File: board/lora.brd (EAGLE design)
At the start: 20.2 x 72.9 mm, 29 parts, among them J1 SWD_PTH_SHROUD, X1 SMA-142-0701-801/806

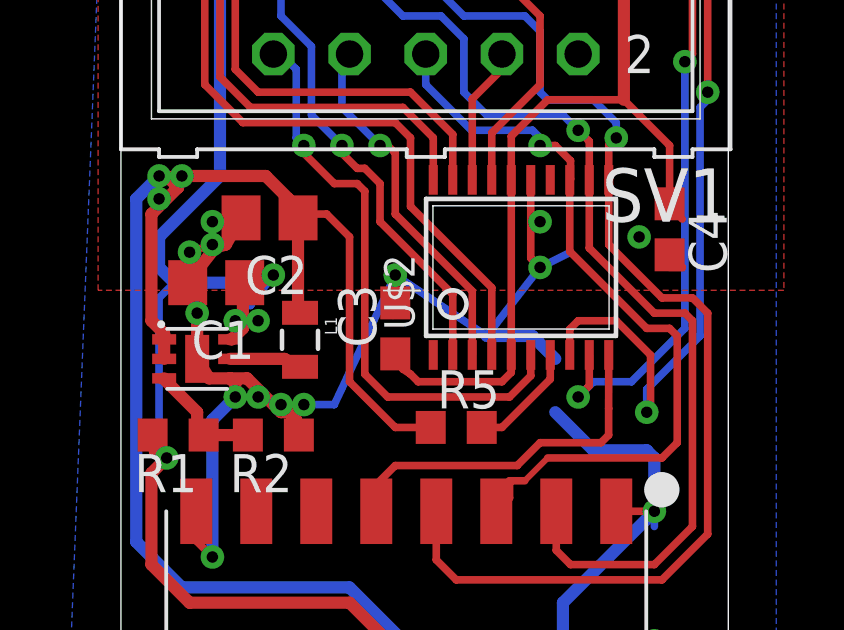
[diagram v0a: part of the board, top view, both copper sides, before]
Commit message: added boot0 to tracker, some wiring on basestation
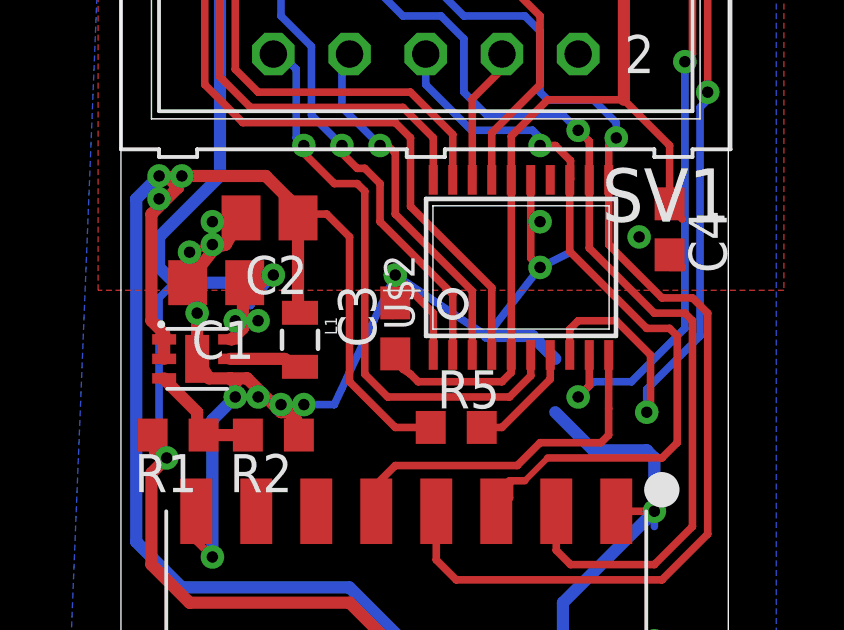
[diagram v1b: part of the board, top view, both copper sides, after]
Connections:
- net GND: now also U$2.1
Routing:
- net GND: track 95.3 -> 98.5 mm
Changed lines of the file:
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@@
 <via x="15.875" y="48.387" extent="1-16" drill="0.381" shape="octagon"/>
 <contactref element="TP2" pad="TP"/>
+<contactref element="U$2" pad="1"/>
+<wire x1="10.41" y1="31.8802" x2="10.41" y2="33.278" width="0.254" layer="1"/>
+<wire x1="10.41" y1="33.278" x2="9.144" y2="34.544" width="0.254" layer="1"/>
 </signal>
 <signal name="N$6">

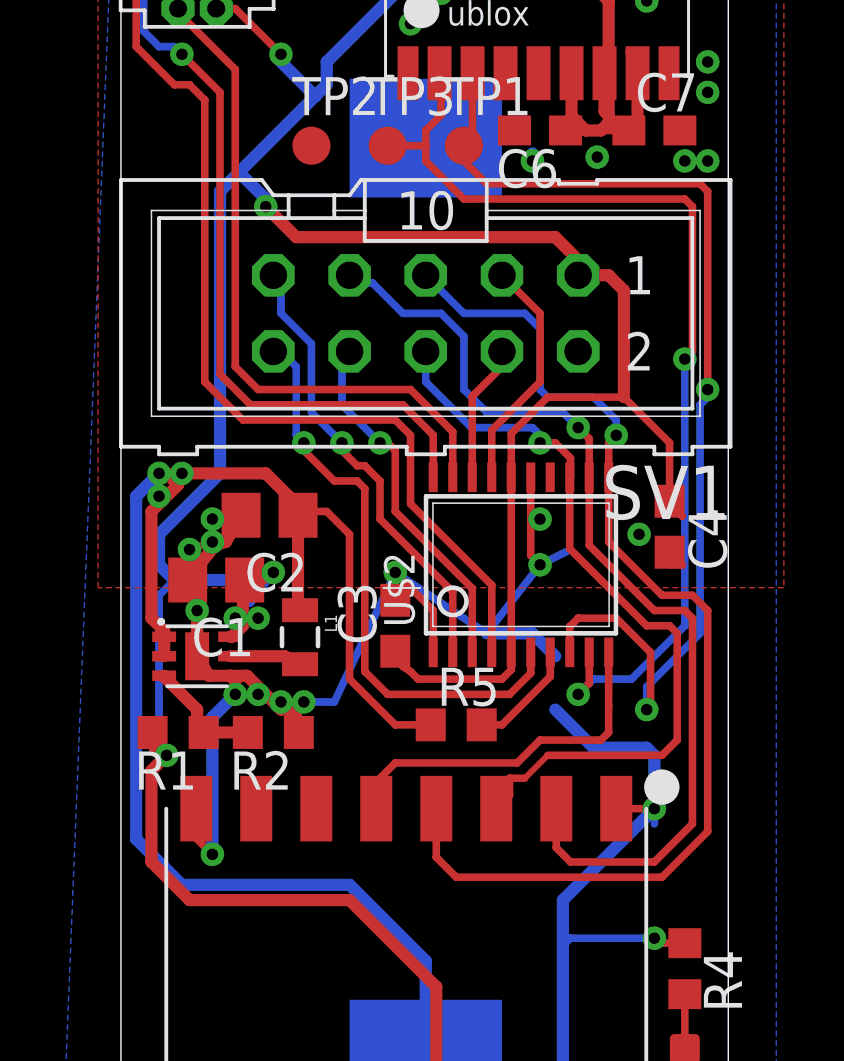
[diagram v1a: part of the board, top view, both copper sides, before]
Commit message: initial route
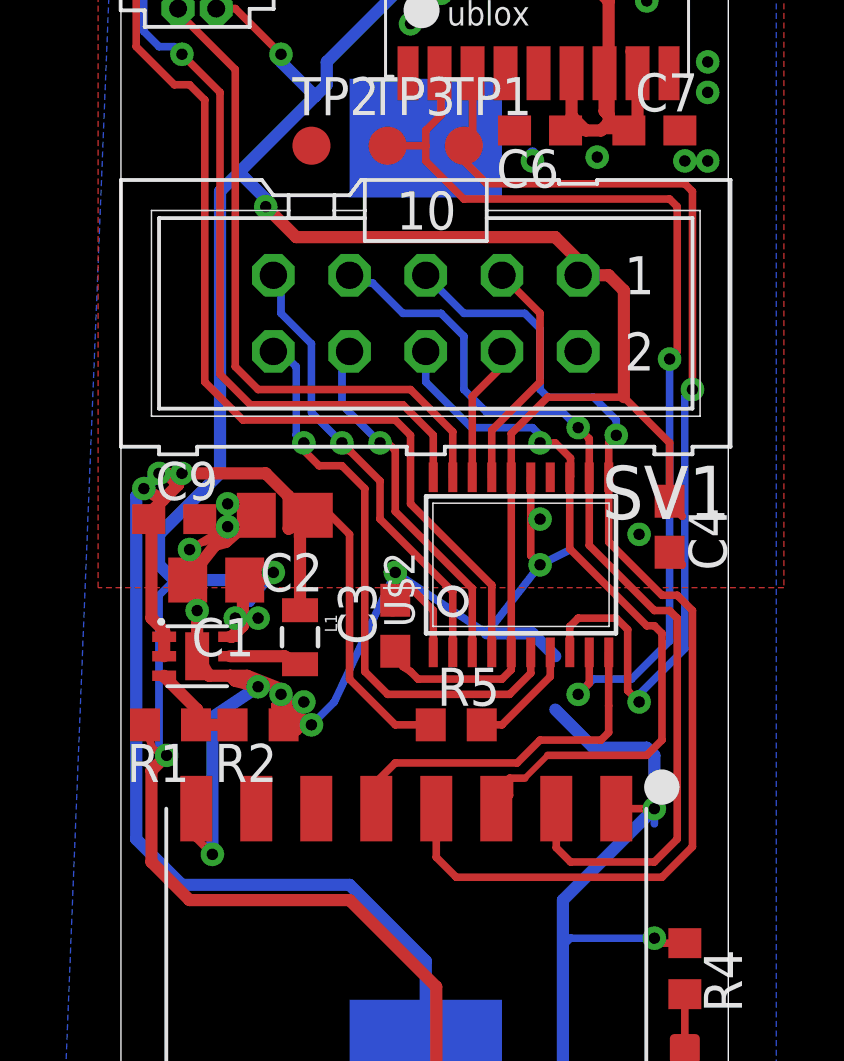
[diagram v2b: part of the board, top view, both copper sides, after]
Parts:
- added C9: (no value), rcl:C0603
- moved R2 0.57 mm to (4.57, 29.5)
- moved C2 0.51 mm to (5.46, 36.4)
- moved R1 0.36 mm to (1.65, 29.5)
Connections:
- net GND: now also C9.2
- net VBAT: now also C9.1
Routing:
- net GND: track 98.5 -> 103.6 mm
- net VBAT: track 66.7 -> 68.3 mm
- net UART_TX: track 35.8 -> 34.5 mm
- net MOSI: track 26.5 -> 25.4 mm
- net MISO: track 32.7 -> 32.0 mm
- net UART_RX: track 34.1 -> 33.4 mm
- net SCLK: track 36.9 -> 36.2 mm
- net N$6: track 3.91 -> 3.41 mm

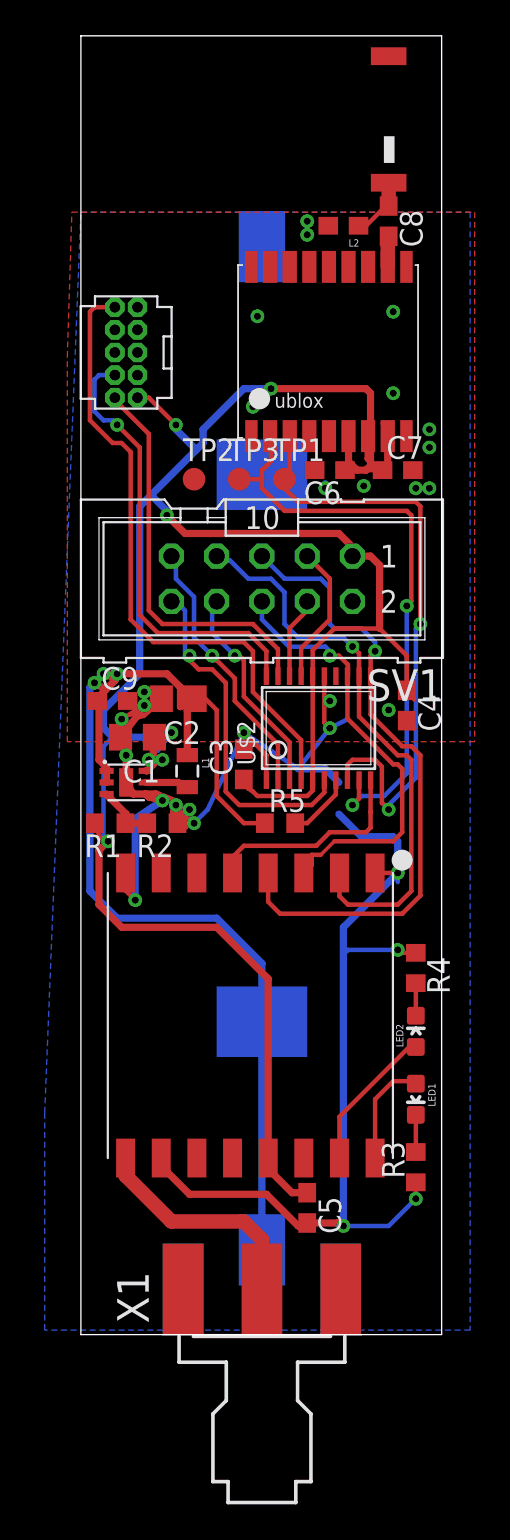
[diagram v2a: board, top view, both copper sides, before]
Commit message: adding interrupt line to raido
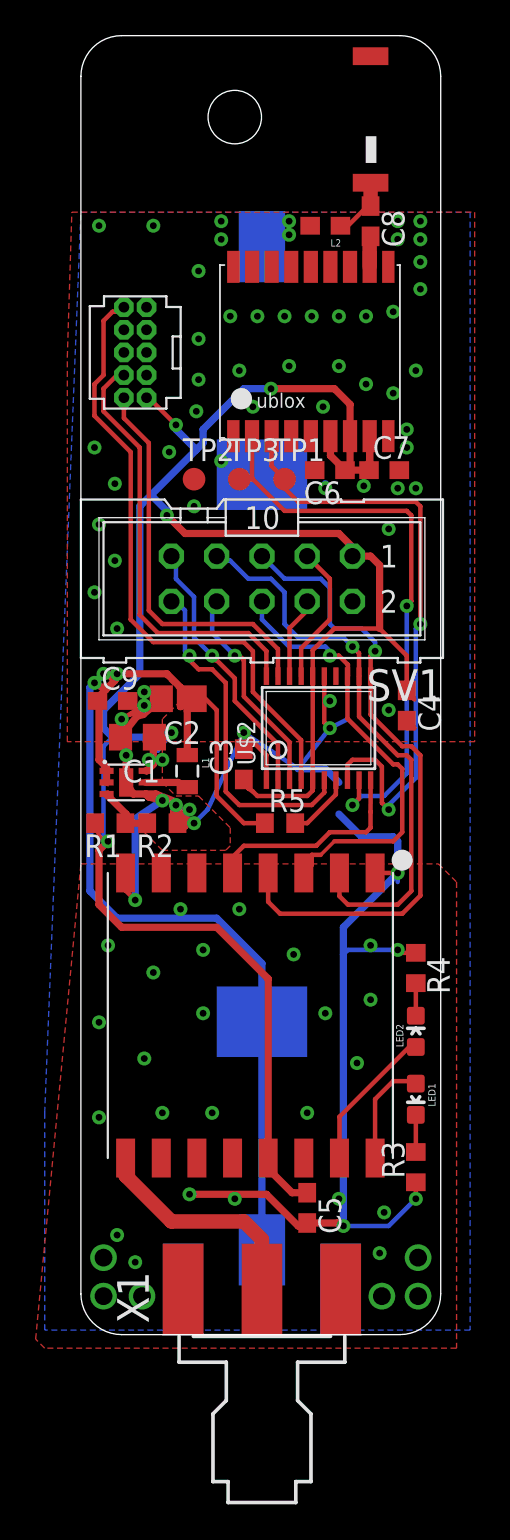
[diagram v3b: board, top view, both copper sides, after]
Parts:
- moved L2 1.02 mm to (13.7, 63.0)
- moved U$3 1.02 mm to (13.0, 56.1)
- moved C8 1.02 mm to (16.3, 63.2)
- moved U$4 1.02 mm to (16.3, 68.6)
- moved C7 0.76 mm to (17.0, 49.3)
- moved J1 0.51 mm to (3.05, 55.9)
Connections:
- net GND: now also X1.G@1, X1.G@2, X1.G@3, X1.G@4
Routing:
- net +3V3: track 133.4 -> 130.1 mm
- net GND: track 103.6 -> 101.5 mm, vias 29 -> 95
- net SWCLK: track 25.2 -> 24.4 mm, vias 1 -> 0
- net RST: track 36.0 -> 35.2 mm
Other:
- outline, holes or cut-outs redrawn

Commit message: some stuff changed lol
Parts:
- added L3: (no value), SparkFun-Passives:1210
- added S1: SWITCH-MOMENTARY-2SMD, Mine:TACTILE_SWITCH_SMD
- moved R3 11.2 mm to (18.8, 21.3)
- moved R4 11.2 mm to (18.8, 10.2), turned to 90 degrees
- moved LED1 3.81 mm to (18.8, 17.8)
- moved LED2 3.81 mm to (18.8, 14.0), turned to 180 degrees
- moved R2 1.02 mm to (3.56, 29.5)
- moved L1 0.76 mm to (5.97, 33.1)
- moved R1 0.74 mm to (1.02, 29.1), turned to 270 degrees
- moved C1 0.51 mm to (2.67, 34.3)
- moved U$7 0.51 mm to (2.03, 31.8)
- moved C4 0.25 mm to (18.3, 36.3)
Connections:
- removed net N$12: LED1.A, U$6.16
- net +3V3: now also LED2.A
- net GND: now also LED1.C, S1.1; no longer R3.1, R4.1
- net N$3: now also L3.2
- net N$5: now also LED1.A, R3.1, S1.3; no longer LED1.C, R3.2
- net N$8: now also R3.2, R4.1, U$2.14; no longer LED2.A, U$6.15
- net VBAT: now also L3.1
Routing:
- net GND: track 101.5 -> 52.9 mm, vias 95 -> 96
- net N$8: track 8.22 -> 36.7 mm, vias 0 -> 3
- net +3V3: track 130.1 -> 145.5 mm
- net N$12: track 6.06 -> 0.00 mm
- net N$5: track 2.08 -> 7.88 mm, vias 0 -> 1
- net UART_TX: track 34.7 -> 31.7 mm
- net UART_RX: track 33.2 -> 31.5 mm
- net N$3: track 2.39 -> 3.66 mm
- net VBAT: track 68.3 -> 67.3 mm
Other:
- outline, holes or cut-outs redrawn

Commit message: adding stuff to silk
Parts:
- removed SV1: (no value), con-ml:ML10
- added JP1: M05X2SHD, SparkFun-Connectors:2X5-SHROUDED
- added X3: RFM98, Mine:RFM97
- C1: value (none) -> 4u7; device rcl:C0805 -> rcl:C0603
- C2: value (none) -> 100n; device rcl:C0805 -> rcl:C0603
- C3, C6: value (none) -> 10u; device rcl:C0603 -> rcl:C0805
- C4, C5, C7: value (none) -> 1u
- C8: value (none) -> 100n
- L1: value (none) -> 2u2
- R1, R2: value (none) -> 330
- R3: value (none) -> 360k
- R4: value (none) -> 220k
- R5: value (none) -> 10k
- U$1: value KEYSTONE-53 -> (none); device Mine:KEYSTONE53 -> Mine:SUSF-XSM
- U$6: value RFM98 -> KEYSTONE-53; device Mine:RFM97 -> Mine:KEYSTONE53
- moved C9 30.6 mm to (16.3, 63.2), turned to 270 degrees
- moved C5 29.0 mm to (18.3, 36.3)
- moved C1 28.3 mm to (12.7, 7.87), turned to 270 degrees
- moved R1 26.0 mm to (18.8, 10.2), turned to 90 degrees
- moved R4 24.6 mm to (3.56, 29.5), turned to 180 degrees
- moved R3 19.4 mm to (1.02, 29.1), turned to 270 degrees
- moved R2 17.3 mm to (18.8, 21.3), turned to 90 degrees
- moved C4 16.5 mm to (1.78, 36.3), turned to 0 degrees
- moved C6 15.4 mm to (5.46, 36.4)
- moved C8 14.0 mm to (17.0, 49.3), turned to 0 degrees
- moved U$6 9.92 mm to (10.2, 34.3), flipped to the bottom, turned to 90 degrees
- moved U$1 7.85 mm to (17.0, 30.5), turned to 0 degrees
- moved C3 6.65 mm to (2.67, 34.3), turned to 180 degrees
- moved C2 5.21 mm to (9.14, 32.8), turned to 90 degrees
- moved TP1 5.08 mm to (6.35, 48.8)
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- renumbered U$2 to IC1, U$3 to X2, U$4 to U$5, U$7 to IC2
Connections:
- net +3V3: now also C2.1, C8.1, JP1.1, LED1.A, R3.2, X3.13; no longer C4.1, C6.1, LED2.A, R1.2, SV1.1, U$6.13
- net GND: now also C8.2, JP1.2, LED2.C, R4.1, TP1.TP, U$6.N1, U$6.N2, X3.1, X3.10, X3.8; no longer C9.2, LED1.C, R2.1, SV1.2, TP2.TP, U$1.N1, U$1.N2, U$6.1, U$6.10, U$6.8
- net GPIO1: now also JP1.8; no longer SV1.8
- net GPIO2: now also JP1.9; no longer SV1.9
- net GPIO3: now also JP1.10; no longer SV1.10
- net MISO: now also JP1.7, X3.2; no longer SV1.7, U$6.2
- net MOSI: now also JP1.6, X3.3; no longer SV1.6, U$6.3
- net N$1: now also C9.2; no longer C8.2
- net N$2: now also X3.9; no longer U$6.9
- net N$4: now also C9.1; no longer C8.1
- net N$5: now also LED2.A, R2.1; no longer LED1.A, R3.1
- net N$6: now also R3.1, R4.2; no longer R1.1, R2.2
- net N$7: now also LED1.C, R1.2; no longer LED2.C, R4.2
- net N$8: now also R1.1, R2.2; no longer R3.2, R4.1
- net NSS: now also X3.5; no longer U$6.5
- net SCL: now also JP1.3; no longer SV1.3
- net SCLK: now also JP1.5, X3.4; no longer SV1.5, U$6.4
- net SDA: now also JP1.4; no longer SV1.4
- net UART_RX: now also TP2.TP; no longer TP3.TP
- net UART_TX: now also TP3.TP; no longer TP1.TP
- net VBAT: now also C4.1, C6.1, U$6.P1, U$6.P2; no longer C2.1, C9.1, U$1.P1, U$1.P2
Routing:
- net VBAT: track 67.3 -> 71.6 mm
- net +3V3: track 145.5 -> 144.8 mm
- net GND: vias 96 -> 100
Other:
- outline, holes or cut-outs redrawn
- board text added: "GND"
- board text added: "Matt Brejza"
- board text added: "R"
- board text added: "Sept 14"
- board text added: "T"

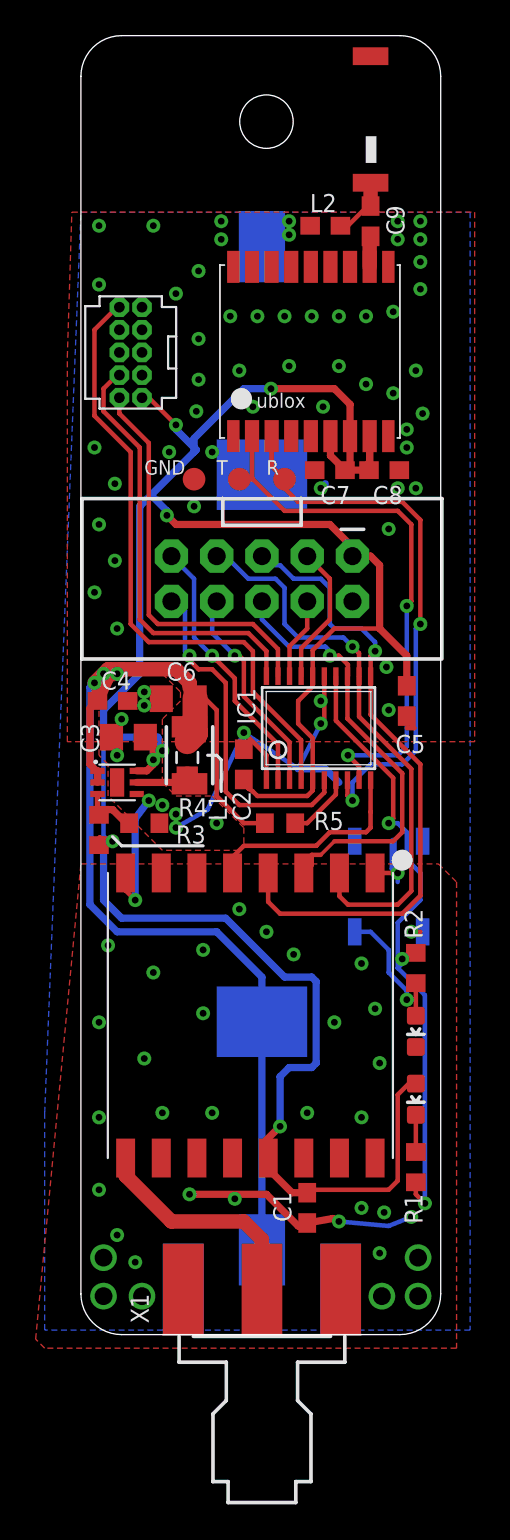
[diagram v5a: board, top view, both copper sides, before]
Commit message: connecting clkout
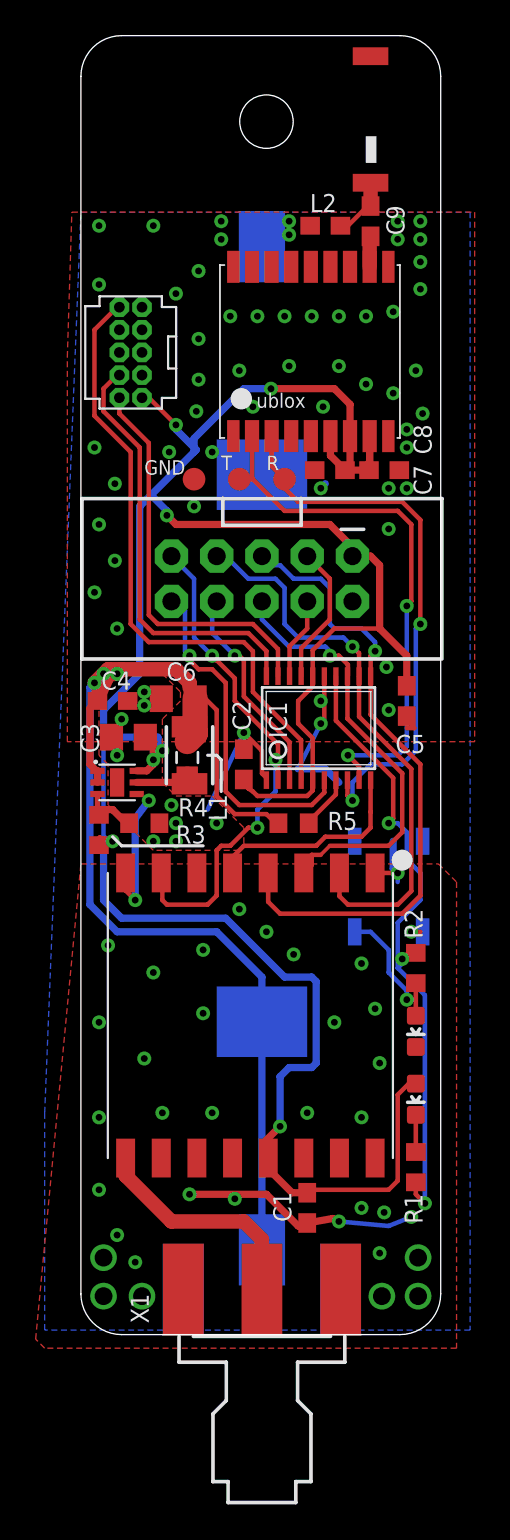
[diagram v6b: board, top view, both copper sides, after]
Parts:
- moved R5 0.76 mm to (11.9, 29.5)
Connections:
- new net N$10: X3.6
- net GPIO2: now also X3.7
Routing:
- net GPIO2: track 15.2 -> 29.8 mm, vias 1 -> 3
- net GND: track 52.9 -> 47.2 mm, vias 100 -> 101
- net VBAT: track 71.6 -> 72.4 mm
- net N$9: track 3.76 -> 3.17 mm

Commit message: adding copyright notice
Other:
- board text added: "©"
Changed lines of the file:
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@@
 <grid distance="10" unitdist="mil" unit="mil" style="lines" multiple="1" display="no" altdistance="5" altunitdist="mil" altunit="mil"/>
 <layers>
-<layer number="1" name="Top" color="4" fill="1" visible="yes" active="yes"/>
+<layer number="1" name="Top" color="4" fill="1" visible="no" active="yes"/>
 <layer number="16" name="Bottom" color="1" fill="1" visible="yes" active="yes"/>
 <layer number="17" name="Pads" color="2" fill="1" visible="yes" active="yes"/>
@@
 <layer number="19" name="Unrouted" color="6" fill="1" visible="yes" active="yes"/>
 <layer number="20" name="Dimension" color="15" fill="1" visible="yes" active="yes"/>
-<layer number="21" name="tPlace" color="7" fill="1" visible="yes" active="yes"/>
-<layer number="22" name="bPlace" color="7" fill="1" visible="no" active="yes"/>
+<layer number="21" name="tPlace" color="7" fill="1" visible="no" active="yes"/>
+<layer number="22" name="bPlace" color="7" fill="1" visible="yes" active="yes"/>
 <layer number="23" name="tOrigins" color="15" fill="1" visible="yes" active="yes"/>
 <layer number="24" name="bOrigins" color="15" fill="1" visible="yes" active="yes"/>
-<layer number="25" name="tNames" color="7" fill="1" visible="yes" active="yes"/>
-<layer number="26" name="bNames" color="7" fill="1" visible="no" active="yes"/>
-<layer number="27" name="tValues" color="7" fill="1" visible="yes" active="yes"/>
-<layer number="28" name="bValues" color="7" fill="1" visible="no" active="yes"/>
-<layer number="29" name="tStop" color="7" fill="3" visible="yes" active="yes"/>
+<layer number="25" name="tNames" color="7" fill="1" visible="no" active="yes"/>
+<layer number="26" name="bNames" color="7" fill="1" visible="yes" active="yes"/>
+<layer number="27" name="tValues" color="7" fill="1" visible="no" active="yes"/>
+<layer number="28" name="bValues" color="7" fill="1" visible="yes" active="yes"/>
+<layer number="29" name="tStop" color="7" fill="3" visible="no" active="yes"/>
 <layer number="30" name="bStop" color="7" fill="6" visible="yes" active="yes"/>
 <layer number="31" name="tCream" color="7" fill="4" visible="no" active="yes"/>
@@
 <text x="13.716" y="27.94" size="1.016" layer="22" font="vector" ratio="13" rot="MR0">Sept 14</text>
 <text x="13.716" y="26.67" size="1.016" layer="22" font="vector" ratio="13" rot="MR0">Matt Brejza</text>
+<text x="3.81" y="26.416" size="1.27" layer="22" rot="MR0">©</text>
 </plain>
 <attributes>
